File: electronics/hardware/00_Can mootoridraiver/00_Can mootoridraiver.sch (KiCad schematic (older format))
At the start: 6 parts

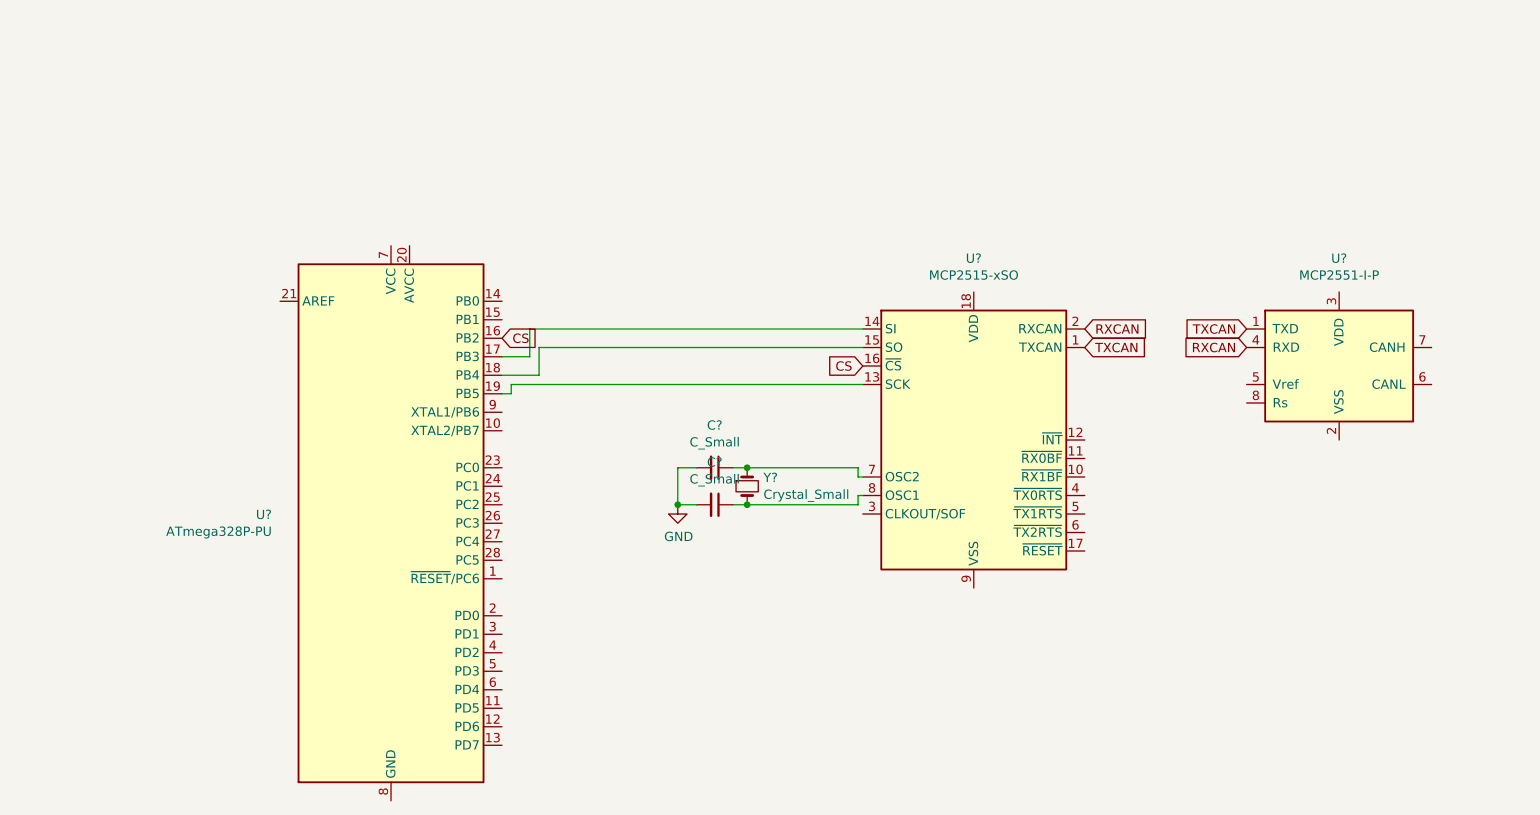
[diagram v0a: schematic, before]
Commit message: Uuendatud skeem uue CAN driveri kiibiga
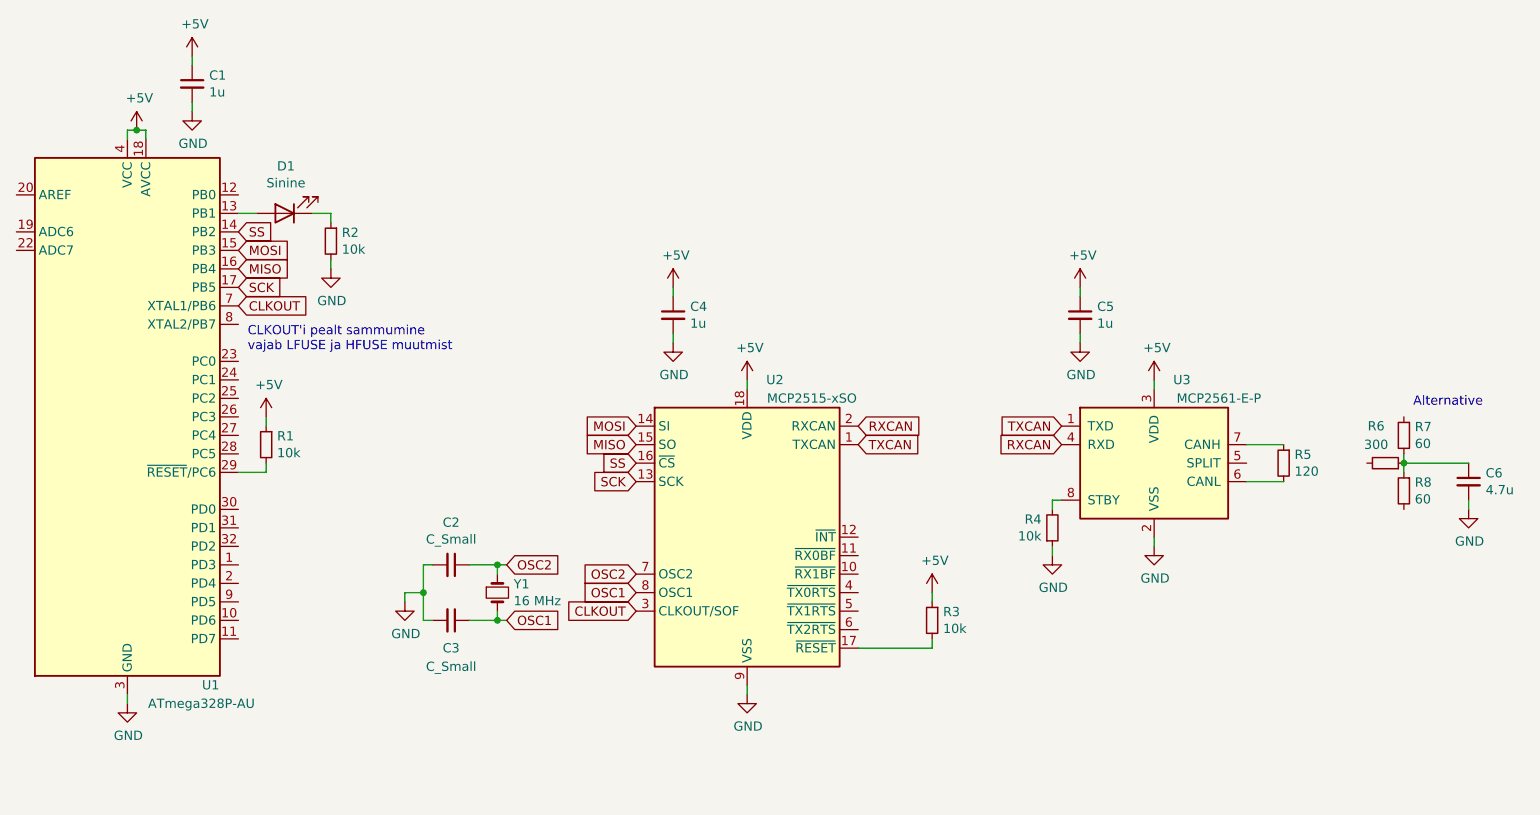
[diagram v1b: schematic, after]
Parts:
- removed C? (x2): C_Small, symbol Device:C_Small
- removed U?: ATmega328P-PU, Package_DIP:DIP-28_W7.62mm, symbol MCU_Microchip_ATmega:ATmega328P-PU
- removed U?: MCP2551-I-P, Package_DIP:DIP-8_W7.62mm, symbol Interface_CAN_LIN:MCP2551-I-P
- removed U?: MCP2515-xSO, Package_SO:SOIC-18W_7.5x11.6mm_P1.27mm, symbol Interface_CAN_LIN:MCP2515-xSO
- removed Y?: Crystal_Small, symbol Device:Crystal_Small
- added C1, C4, C5: 1u, symbol Device:C_Small
- added C2, C3: C_Small, symbol Device:C_Small
- added C6: 4.7u, symbol Device:C_Small
- added D1: Sinine, symbol Device:LED
- added R1, R2, R3, R4: 10k, symbol Device:R_Small
- added R5: 120, symbol Device:R_Small
- added R6: 300, symbol Device:R_Small
- added R7, R8: 60, symbol Device:R_Small
- added U1: ATmega328P-AU, Package_QFP:TQFP-32_7x7mm_P0.8mm, symbol MCU_Microchip_ATmega:ATmega328P-AU
- added U2: MCP2515-xSO, Package_SO:SOIC-18W_7.5x11.6mm_P1.27mm, symbol Interface_CAN_LIN:MCP2515-xSO
- added U3: MCP2561-E-P, symbol Interface_CAN_LIN:MCP2561-E-SN
- added Y1: 16 MHz, symbol Device:Crystal_Small
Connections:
- net GND: now also C1.2, C2.2, C3.2, C4.2, C5.2, C6.2, R2.2, R4.1, U1.21 (GND), U1.3 (GND), U1.5 (GND), U2.9 (VSS), U3.2 (VSS)
- net RXCAN: now also U2.2 (RXCAN), U3.4 (RXD)
- net TXCAN: now also U2.1 (TXCAN), U3.1 (TXD)
- new net: R5.2, U3.6 (CANL)
- new net: R5.1, U3.7 (CANH)
- new net: R4.2, U3.8 (STBY)
- new net: R3.2, U2.17 (~RESET)
- new net: C6.1, R6.1, R7.2, R8.1
- new net: D1.2 (A), U1.13 (PB1)
- new net: R1.2, U1.29 (~RESET~/PC6)
- new net: D1.1 (K), R2.1
- new net +5V: C1.1, C4.1, C5.1, R1.1, R3.1, U1.18 (AVCC), U1.4 (VCC), U1.6 (VCC), U2.18 (VDD), U3.3 (VDD)
- new net CLKOUT: U1.7 (XTAL1/PB6), U2.3 (CLKOUT/SOF)
- new net MISO: U1.16 (PB4), U2.15 (SO)
- new net MOSI: U1.15 (PB3), U2.14 (SI)
- new net OSC1: C3.1, U2.8 (OSC1), Y1.2
- new net OSC2: C2.1, U2.7 (OSC2), Y1.1
- new net SCK: U1.17 (PB5), U2.13 (SCK)
- new net SS: U1.14 (PB2), U2.16 (~CS)
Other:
- note added: "Alternative\n"
- note added: "CLKOUT'i pealt sammumine\nvajab LFUSE ja HFUSE muutmist"

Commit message: CAN driveri footprint
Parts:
- U3: footprint (none) -> Package_SO:SOIC-8_3.9x4.9mm_P1.27mm
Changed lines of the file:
@@
 F 0 "U3" H 8100 3550 50  0000 C CNN
 F 1 "MCP2561-E-P" H 8300 3450 50  0000 C CNN
+F 2 "Package_SO:SOIC-8_3.9x4.9mm_P1.27mm" H 7950 2600 50  0001 C CIN
 F 3 "http://ww1.microchip.com/downloads/en/DeviceDoc/25167A.pdf" H 7950 3100 50  0001 C CNN
 	1    7950 3100
